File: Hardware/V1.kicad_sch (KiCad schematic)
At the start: 35 parts, among them U1 ADS1298xPAG, U2 ESP32-S3, U3 ADS1298xPAG

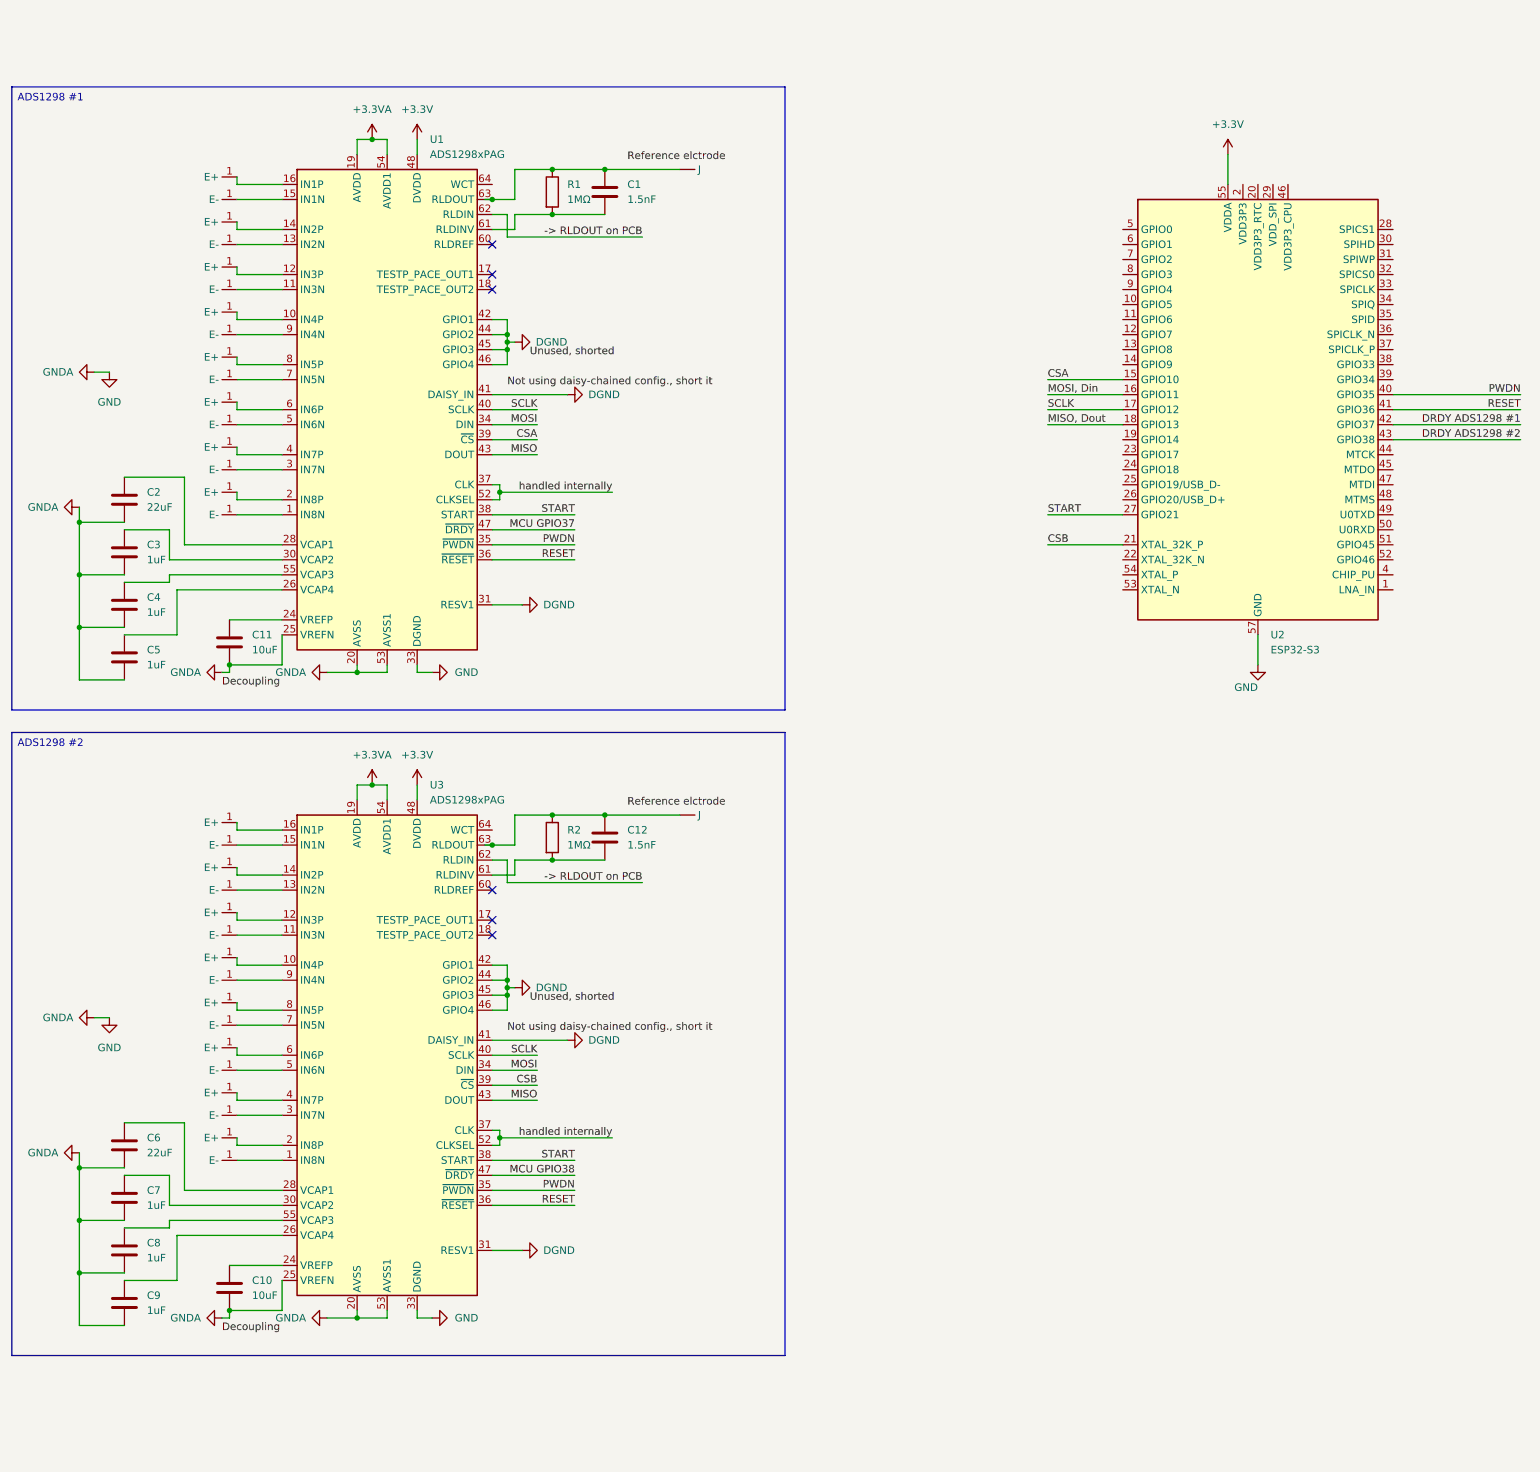
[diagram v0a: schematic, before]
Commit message: Update on KiCad Circuit Schematic of ESP32-S3
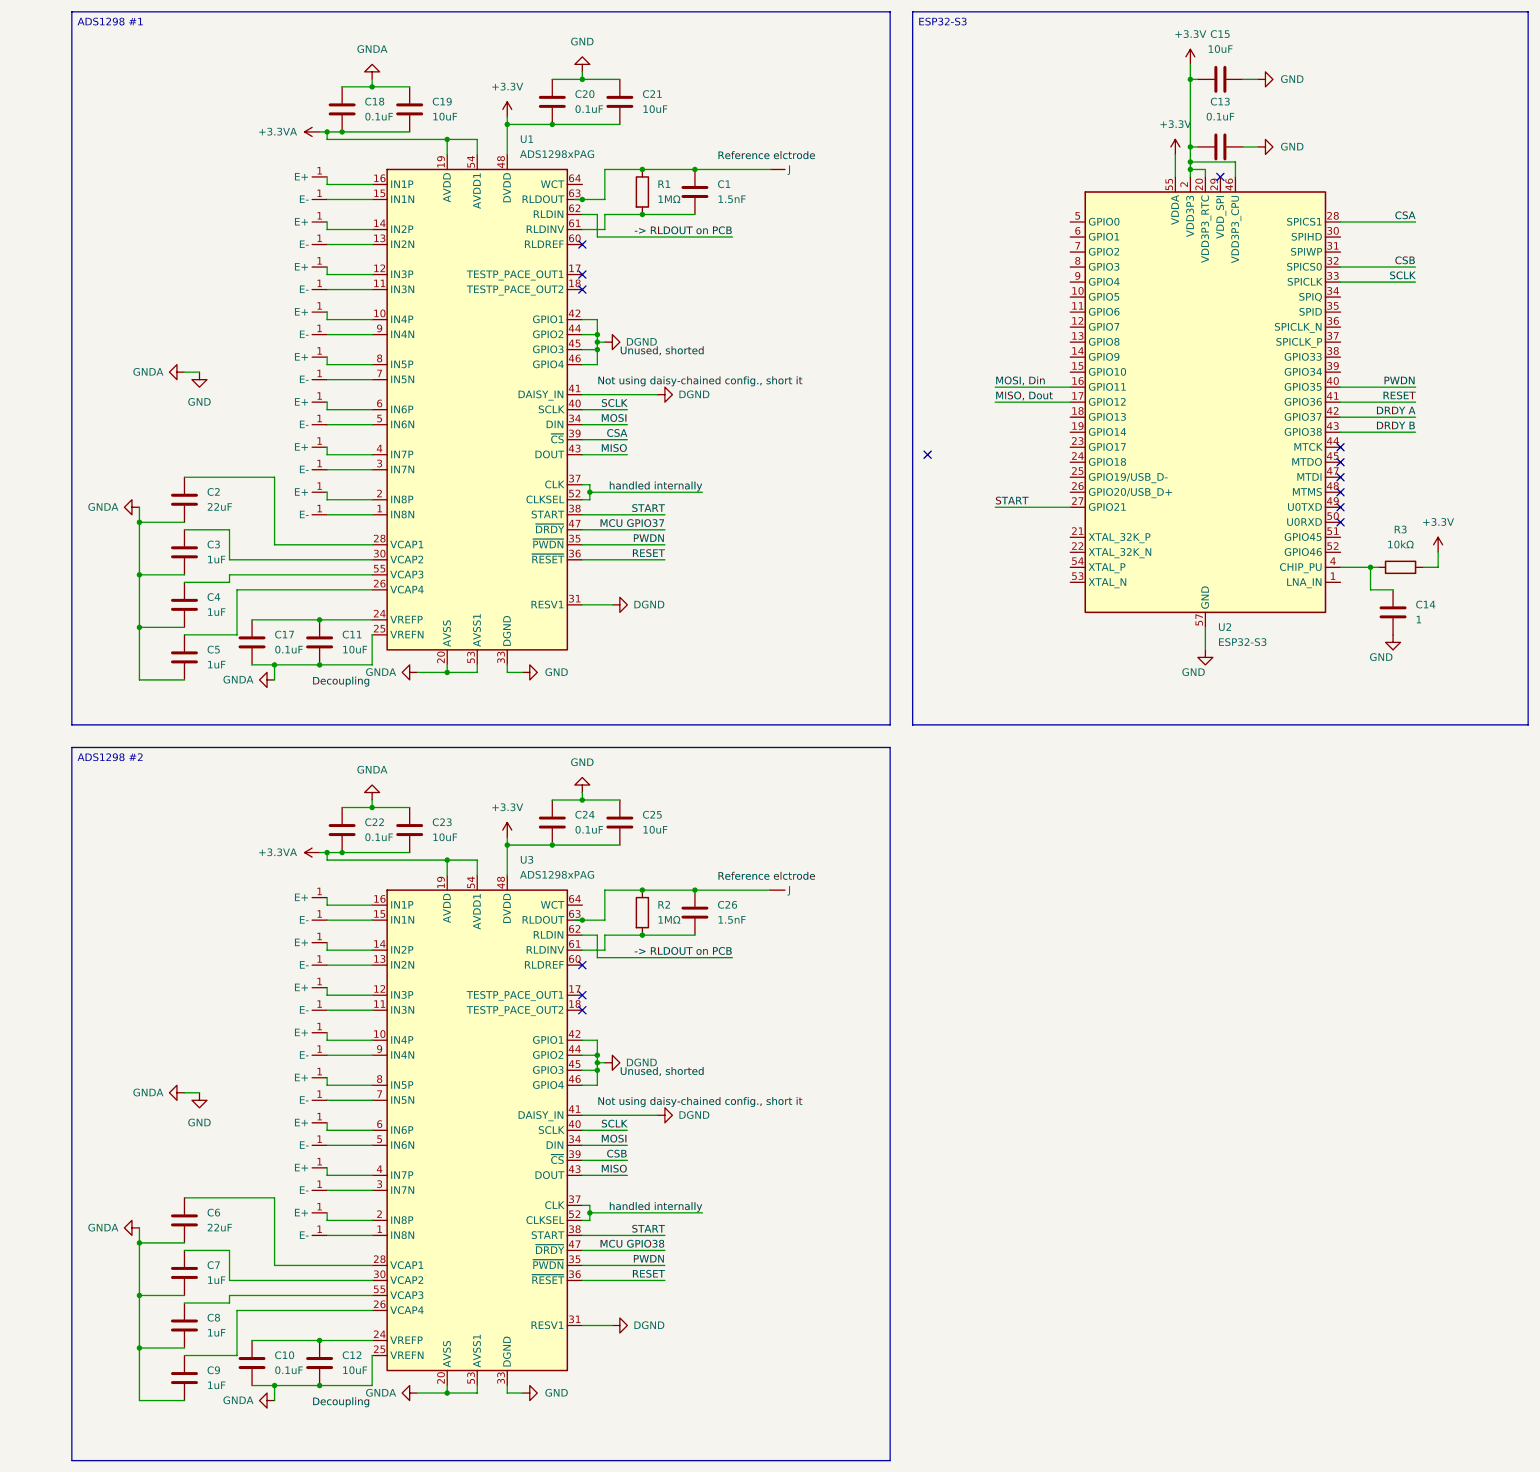
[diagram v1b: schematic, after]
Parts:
- added C13, C17, C18, C20, C22, C24: 0.1uF, symbol Device:C
- added C14: 1, symbol Device:C
- added C15, C19, C21, C23, C25: 10uF, symbol Device:C
- added C26: 1.5nF, symbol Device:C
- added R3: 10kΩ, symbol Device:R
- C10: value 10uF -> 0.1uF
- C12: value 1.5nF -> 10uF
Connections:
- net +3.3V: now also U2.2 (VDD3P3), U2.20 (VDD3P3_RTC), U2.3 (VDD3P3), U2.46 (VDD3P3_CPU), C13.1, C15.1, C20.2, C21.2, C24.2, C25.2, R3.2
- net +3.3VA: now also C18.2, C19.2, C22.2, C23.2
- net CSA: now also U2.28 (SPICS1); no longer U2.15 (GPIO10)
- net CSB: now also U2.32 (SPICS0); no longer U2.21 (XTAL_32K_P)
- net GND: now also C12.2, C13.2, C14.2, C15.2, C17.2, C18.1, C19.1, C20.1, C21.1, C22.1, C23.1, C24.1, C25.1
- net MISO, Dout: now also U2.17 (GPIO12); no longer U2.18 (GPIO13)
- net SCLK: now also U2.33 (SPICLK); no longer U2.17 (GPIO12)
- net at U2.4 (CHIP_PU): now also C14.1, R3.1
- net at R2.1, U3.63 (RLDOUT), U5. (J): now also C26.1; no longer C12.1
- net at R2.2, U3.61 (RLDINV): now also C26.2; no longer C12.2
- net at C10.1, U3.24 (VREFP): now also C12.1
- net at C11.1, U1.24 (VREFP): now also C17.1
- net DRDY ADS1298 #1 renamed DRDY A
- net DRDY ADS1298 #2 renamed DRDY B
- no-connect marks 6 -> 14
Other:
- moved on the sheet: C1, C11, C2, C3, C4, C5, R1, U1, U2

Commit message: Update on minor change
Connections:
- no-connect marks 14 -> 13
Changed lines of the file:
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@@
-	)
-	(no_connect
-		(at 203.2 93.98)
 	)
 	(no_connect

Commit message: [docs] Upload Cicruit Schematic Draft 1
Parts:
- C14: value 1 -> 1uF
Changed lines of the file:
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@@
 			)
 		)
-		(property "Value" "1"
+		(property "Value" "1uF"
 			(at 285.75 121.9199 0)
 			(effects
